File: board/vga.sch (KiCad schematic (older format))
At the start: 19 parts, among them P501 VGA RX I2C 3v, P502 VGA TX I2C 3v, P503 VGA RX I2C 5v, P504 VGA TX I2C 5v, P505 DE-15, P506 DE-15, P601 3-RCA, U501 TCA9617A, U502 TCA9617A

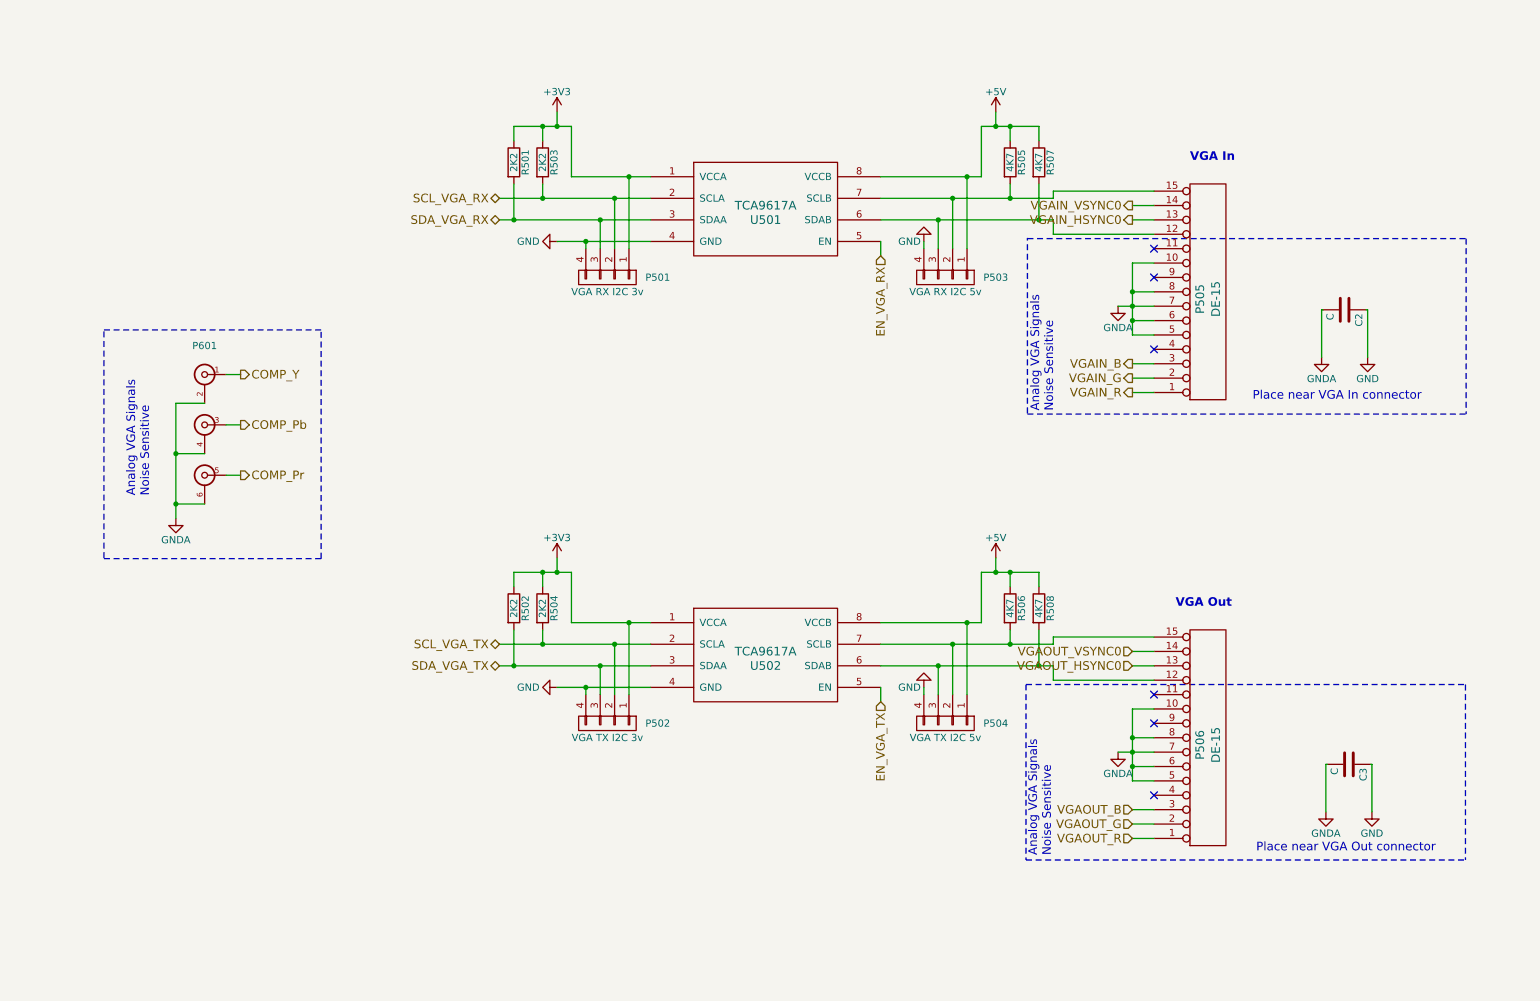
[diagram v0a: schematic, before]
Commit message: Updating net names.
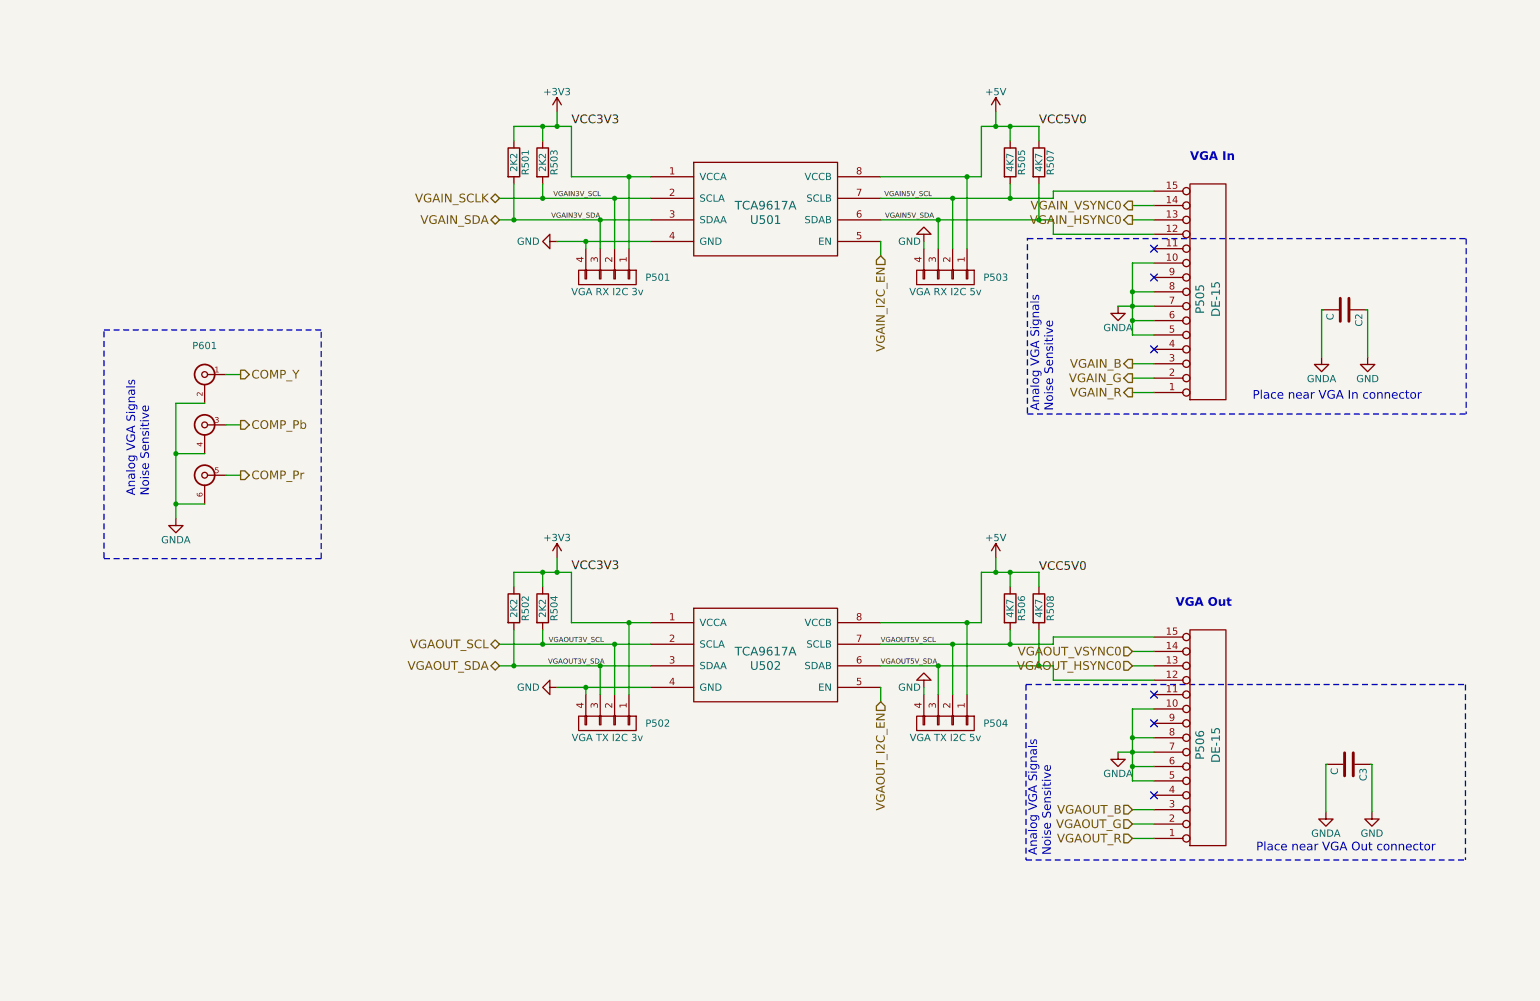
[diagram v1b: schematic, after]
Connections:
- net VGAOUT5V_SDA: now reaches P504.3 (P3), P506.12 (P12), R508.2, U502.6 (SDAB)
- net VGAOUT5V_SCL: now reaches P504.2 (P2), P506.15 (P15), R506.2, U502.7 (SCLB)
- net VGAIN5V_SDA: now reaches P503.3 (P3), P505.12 (P12), R507.2, U501.6 (SDAB)
- net VGAIN5V_SCL: now reaches P503.2 (P2), P505.15 (P15), R505.2, U501.7 (SCLB)
- net EN_VGA_RX renamed VGAIN_I2C_EN
- net EN_VGA_TX renamed VGAOUT_I2C_EN
- net SCL_VGA_RX renamed VGAIN_SCLK
- net SCL_VGA_TX renamed VGAOUT_SCL
- net SDA_VGA_RX renamed VGAIN_SDA
- net SDA_VGA_TX renamed VGAOUT_SDA
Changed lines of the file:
@@
 $EndDescr
 Text HLabel 3900 4900 0    60   BiDi ~ 0
-SCL_VGA_TX
+VGAOUT_SCL
 Text HLabel 3900 5050 0    60   BiDi ~ 0
-SDA_VGA_TX
+VGAOUT_SDA
 $Comp
 L TCA9617A U502
@@
 VGAOUT_R
 $Comp
-L GNDA #PWR044
+L GNDA #PWR54
 U 1 1 563F8497
 P 8200 5650
-F 0 "#PWR044" H 8200 5400 50  0001 C CNN
+F 0 "#PWR54" H 8200 5400 50  0001 C CNN
 F 1 "GNDA" H 8200 5500 50  0000 C CNN
 F 2 "" H 8200 5650 60  0000 C CNN
@@
 $EndComp
 $Comp
-L GND #PWR045
+L GND #PWR48
 U 1 1 563F85E4
 P 4300 5200
-F 0 "#PWR045" H 4300 4950 50  0001 C CNN
+F 0 "#PWR48" H 4300 4950 50  0001 C CNN
 F 1 "GND" V 4300 5000 50  0000 C CNN
 F 2 "" H 4300 5200 60  0000 C CNN
@@
 Connection ~ 7350 4400
 Text HLabel 3900 1800 0    60   BiDi ~ 0
-SCL_VGA_RX
+VGAIN_SCLK
 Text HLabel 3900 1950 0    60   BiDi ~ 0
-SDA_VGA_RX
+VGAIN_SDA
 $Comp
 L TCA9617A U501
@@
 VGAIN_R
 $Comp
-L GNDA #PWR046
+L GNDA #PWR53
 U 1 1 5641B8E6
 P 8200 2550
-F 0 "#PWR046" H 8200 2300 50  0001 C CNN
+F 0 "#PWR53" H 8200 2300 50  0001 C CNN
 F 1 "GNDA" H 8200 2400 50  0000 C CNN
 F 2 "" H 8200 2550 60  0000 C CNN
@@
 $EndComp
 $Comp
-L GND #PWR047
+L GND #PWR46
 U 1 1 5641B8EC
 P 4300 2100
-F 0 "#PWR047" H 4300 1850 50  0001 C CNN
+F 0 "#PWR46" H 4300 1850 50  0001 C CNN
 F 1 "GND" V 4300 1900 50  0000 C CNN
 F 2 "" H 4300 2100 60  0000 C CNN
@@
 Connection ~ 7350 1300
 $Comp
-L +3V3 #PWR048
+L +3V3 #PWR47
 U 1 1 5641A682
 P 4300 4300
-F 0 "#PWR048" H 4300 4150 50  0001 C CNN
+F 0 "#PWR47" H 4300 4150 50  0001 C CNN
 F 1 "+3V3" H 4300 4440 50  0000 C CNN
 F 2 "" H 4300 4300 60  0000 C CNN
@@
 $EndComp
 $Comp
-L +3V3 #PWR049
+L +3V3 #PWR45
 U 1 1 5641A73F
 P 4300 1200
-F 0 "#PWR049" H 4300 1050 50  0001 C CNN
+F 0 "#PWR45" H 4300 1050 50  0001 C CNN
 F 1 "+3V3" H 4300 1340 50  0000 C CNN
 F 2 "" H 4300 1200 60  0000 C CNN
@@
 $EndComp
 $Comp
-L +5V #PWR050
+L +5V #PWR51
 U 1 1 56424FD7
 P 7350 1200
-F 0 "#PWR050" H 7350 1050 50  0001 C CNN
+F 0 "#PWR51" H 7350 1050 50  0001 C CNN
 F 1 "+5V" H 7350 1340 50  0000 C CNN
 F 2 "" H 7350 1200 60  0000 C CNN
@@
 $EndComp
 $Comp
-L +5V #PWR051
+L +5V #PWR52
 U 1 1 56425070
 P 7350 4300
-F 0 "#PWR051" H 7350 4150 50  0001 C CNN
+F 0 "#PWR52" H 7350 4150 50  0001 C CNN
 F 1 "+5V" H 7350 4440 50  0000 C CNN
 F 2 "" H 7350 4300 60  0000 C CNN
@@
 $EndComp
 $Comp
-L GND #PWR052
+L GND #PWR49
 U 1 1 5692C822
 P 6850 2100
-F 0 "#PWR052" H 6850 1850 50  0001 C CNN
+F 0 "#PWR49" H 6850 1850 50  0001 C CNN
 F 1 "GND" H 6950 2100 50  0000 C CNN
 F 2 "" H 6850 2100 50  0000 C CNN
@@
 $EndComp
 $Comp
-L GND #PWR053
+L GND #PWR50
 U 1 1 5692D0C6
 P 6850 5200
-F 0 "#PWR053" H 6850 4950 50  0001 C CNN
+F 0 "#PWR50" H 6850 4950 50  0001 C CNN
 F 1 "GND" H 6950 5200 50  0000 C CNN
 F 2 "" H 6850 5200 50  0000 C CNN
@@
 Connection ~ 6950 5050
 Text HLabel 6550 2200 3    60   Input ~ 0
-EN_VGA_RX
+VGAIN_I2C_EN
 Wire Wire Line
 	6550 2100 6550 2200
 Text HLabel 6550 5300 3    60   Input ~ 0
-EN_VGA_TX
+VGAOUT_I2C_EN
 Wire Wire Line
 	6550 5300 6550 5200
@@
 COMP_Pr
 $Comp
-L GNDA #PWR054
+L GNDA #PWR44
 U 1 1 579715ED
 P 1650 4025
-F 0 "#PWR054" H 1650 3775 50  0001 C CNN
+F 0 "#PWR44" H 1650 3775 50  0001 C CNN
 F 1 "GNDA" H 1650 3875 50  0000 C CNN
 F 2 "" H 1650 4025 60  0000 C CNN
@@
 	7560 5180 10615 5180
 $Comp
-L GNDA #PWR055
+L GNDA #PWR55
 U 1 1 579C5DB4
 P 9615 2905
-F 0 "#PWR055" H 9615 2655 50  0001 C CNN
+F 0 "#PWR55" H 9615 2655 50  0001 C CNN
 F 1 "GNDA" H 9615 2755 50  0000 C CNN
 F 2 "" H 9615 2905 60  0000 C CNN
@@
 $EndComp
 $Comp
-L GND #PWR056
+L GND #PWR57
 U 1 1 579C5DBA
 P 9935 2905
-F 0 "#PWR056" H 9935 2655 50  0001 C CNN
+F 0 "#PWR57" H 9935 2655 50  0001 C CNN
 F 1 "GND" H 9935 2755 50  0000 C CNN
 F 2 "" H 9935 2905 60  0000 C CNN
@@
 	9935 2575 9925 2575
 $Comp
-L GNDA #PWR057
+L GNDA #PWR56
 U 1 1 579C600A
 P 9645 6065
-F 0 "#PWR057" H 9645 5815 50  0001 C CNN
+F 0 "#PWR56" H 9645 5815 50  0001 C CNN
 F 1 "GNDA" H 9645 5915 50  0000 C CNN
 F 2 "" H 9645 6065 60  0000 C CNN
@@
 $EndComp
 $Comp
-L GND #PWR058
+L GND #PWR58
 U 1 1 579C6010
 P 9965 6065
-F 0 "#PWR058" H 9965 5815 50  0001 C CNN
+F 0 "#PWR58" H 9965 5815 50  0001 C CNN
 F 1 "GND" H 9965 5915 50  0000 C CNN
 F 2 "" H 9965 6065 60  0000 C CNN
@@
 Wire Notes Line
 	10620 2080 10620 3300
+Text Label 4400 1300 0    60   ~ 0
+VCC3V3
+Text Label 4400 4400 0    60   ~ 0
+VCC3V3
+Text Label 7650 1300 0    60   ~ 0
+VCC5V0
+Text Label 7650 4405 0    60   ~ 0
+VCC5V0
+Text Label 6575 1800 0    35   ~ 0
+VGAIN5V_SCL
+Text Label 6580 1950 0    35   ~ 0
+VGAIN5V_SDA
+Text Label 4605 1800 2    35   ~ 0
+VGAIN3V_SCL
+Text Label 4600 1950 2    35   ~ 0
+VGAIN3V_SDA
+Text Label 4625 4900 2    35   ~ 0
+VGAOUT3V_SCL
+Text Label 4630 5050 2    35   ~ 0
+VGAOUT3V_SDA
+Text Label 6550 4900 0    35   ~ 0
+VGAOUT5V_SCL
+Text Label 6550 5050 0    35   ~ 0
+VGAOUT5V_SDA
 $EndSCHEMATC

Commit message: Lots of small updates.
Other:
- note added: "Component In"

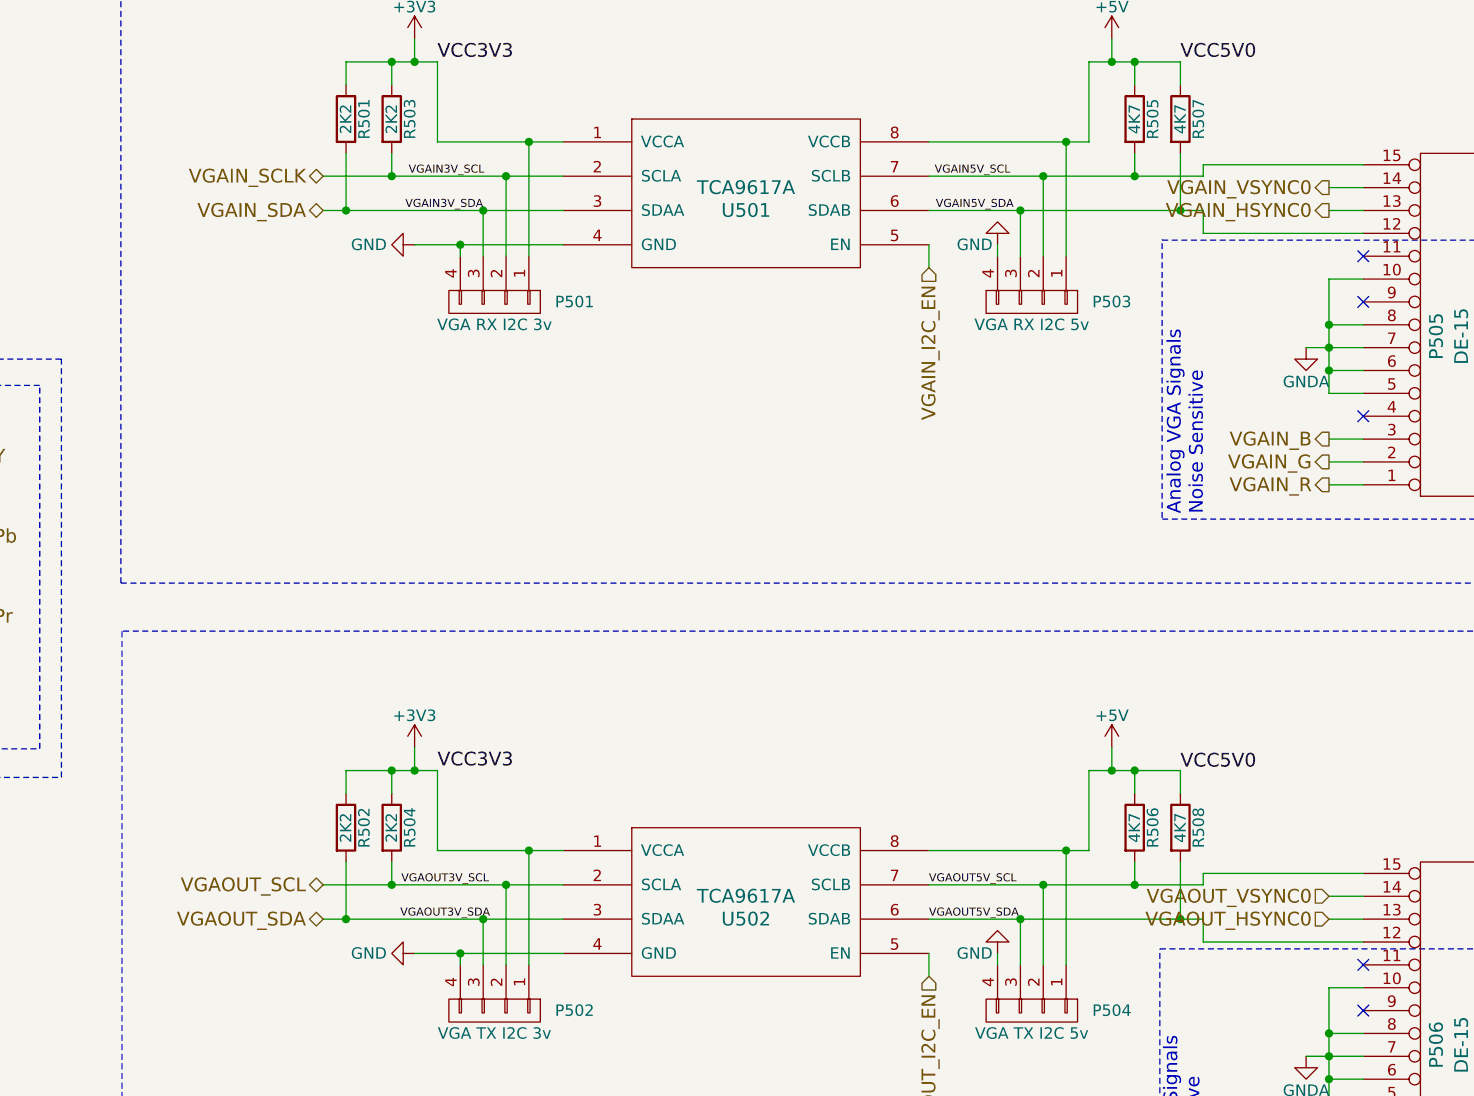
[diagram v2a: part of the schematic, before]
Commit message: ERC and removing 0 from vsync/hsync.
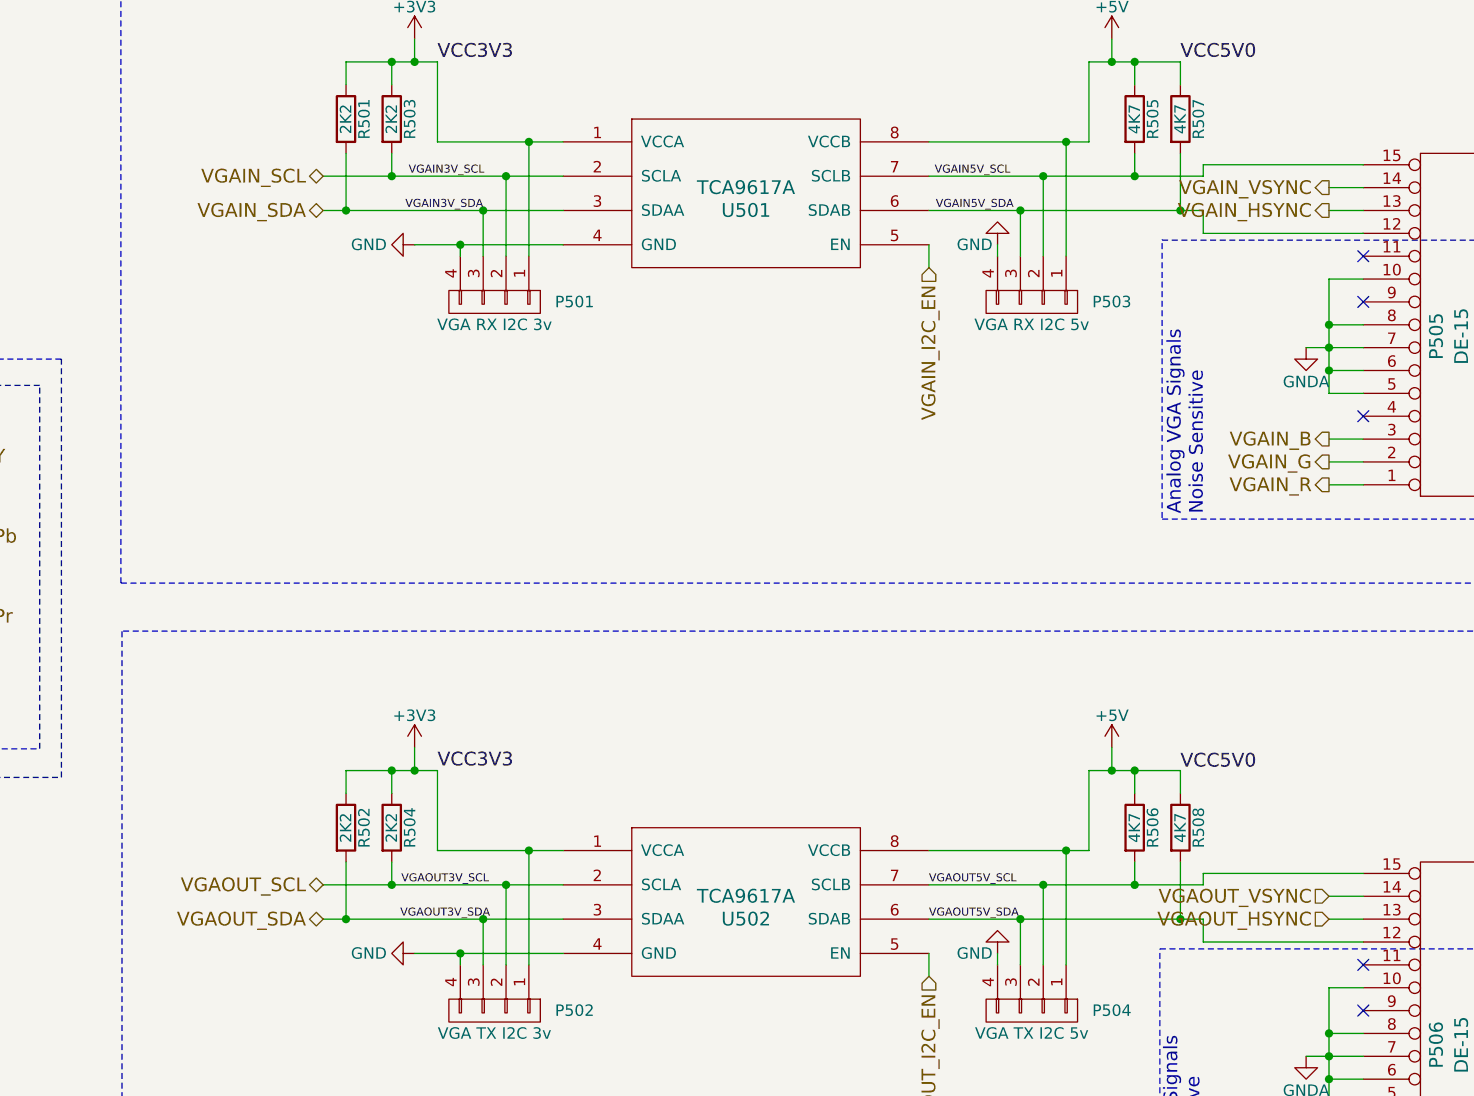
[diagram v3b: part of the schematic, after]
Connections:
- net VGAIN_HSYNC0 renamed VGAIN_HSYNC
- net VGAIN_SCLK renamed VGAIN_SCL
- net VGAIN_VSYNC0 renamed VGAIN_VSYNC
- net VGAOUT_HSYNC0 renamed VGAOUT_HSYNC
- net VGAOUT_VSYNC0 renamed VGAOUT_VSYNC
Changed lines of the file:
@@
 VGA Out
 Text HLabel 8300 5050 0    60   Input ~ 0
-VGAOUT_HSYNC0
+VGAOUT_HSYNC
 Text HLabel 8300 4950 0    60   Input ~ 0
-VGAOUT_VSYNC0
+VGAOUT_VSYNC
 $Comp
 L R R508
@@
 $EndComp
 Text HLabel 3900 1800 0    60   BiDi ~ 0
-VGAIN_SCLK
+VGAIN_SCL
 Text HLabel 3900 1950 0    60   BiDi ~ 0
 VGAIN_SDA
@@
 VGA In
 Text HLabel 8300 1950 0    60   Output ~ 0
-VGAIN_HSYNC0
+VGAIN_HSYNC
 Text HLabel 8300 1850 0    60   Output ~ 0
-VGAIN_VSYNC0
+VGAIN_VSYNC
 $Comp
 L R R507
